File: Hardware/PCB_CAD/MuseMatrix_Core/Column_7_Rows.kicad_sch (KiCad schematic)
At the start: 46 parts, among them J14 Conn_01x03_Pin, J15 Conn_01x07_Socket, J4 Conn_01x07_Socket, Q2 2N3904, Q3 2N3904, Q4 2N3904, Q5 2N3904, Q6 2N3904, Q7 2N3904, Q8 2N3904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

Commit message: more pcb edit
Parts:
- removed J4: Conn_01x07_Socket, Connector_JST:JST_EH_B7B-EH-A_1x07_P2.50mm_Vertical, symbol Connector:Conn_01x07_Socket
- added H1, H2, H3, H4, H5, H6, H7, H8: MountingHole, MountingHole:MountingHole_2.1mm, symbol Mechanical:MountingHole
- added J13: Conn_01x10_Socket, Library:Skedd connector x10, symbol Connector:Conn_01x10_Socket
- added J17, J18: Conn_01x06_Pin, Library:Skedd connector x6, symbol Connector:Conn_01x06_Pin
- J3: renamed from J15; value Conn_01x07_Socket -> Conn_01x10_Socket; footprint Connector_JST:JST_EH_B7B-EH-A_1x07_P2.50mm_Vertical -> Library:Skedd connector x10; symbol Connector:Conn_01x07_Socket -> Connector:Conn_01x10_Socket
- R11, R12, R20, R21, R22, R6: footprint OptoDevice:R_LDR_5.1x4.3mm_P3.4mm_Vertical -> Library:LDR 2.5 horizontal
- R2: renamed from R43; footprint OptoDevice:R_LDR_5.1x4.3mm_P3.4mm_Vertical -> Library:LDR 2.5 horizontal
- R28: footprint Potentiometer_THT:Potentiometer_Bourns_PTV09A-1_Single_Vertical -> Resistor_SMD:R_0402_1005Metric
- renumbered D8 to D1, J14 to J2, Q9 to Q1, R29 to R1
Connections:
- net +3.3V: now also J17.2 (Pin_2), J18.2 (Pin_2)
- net GND: now also J17.1 (Pin_1), J18.1 (Pin_1)
- net column_voltage: now also J17.3 (Pin_3); no longer R17.1, R18.1, R19.1
- net d1: now also J13.1 (Pin_1)
- net d2: now also J13.2 (Pin_2)
- net d3: now also J13.3 (Pin_3)
- net d4: now also J13.4 (Pin_4)
- net d5 renamed d5_0
- net d5_0: now also J18.4 (Pin_4); no longer J3.5 (Pin_5)
- net d6 renamed d6_0
- net d6_0: now also J18.5 (Pin_5); no longer J3.6 (Pin_6)
- net d7 renamed d7_0
- net d7_0: now also J18.6 (Pin_6); no longer J3.7 (Pin_7)
- new net column_voltage2: J18.3 (Pin_3), R17.1, R18.1, R19.1
- new net d5_1: J13.5 (Pin_5), J17.4 (Pin_4), J3.5 (Pin_5)
- new net d6_1: J13.6 (Pin_6), J17.5 (Pin_5), J3.6 (Pin_6)
- new net d7_1: J13.7 (Pin_7), J17.6 (Pin_6), J3.7 (Pin_7)
- no-connect marks 0 -> 3

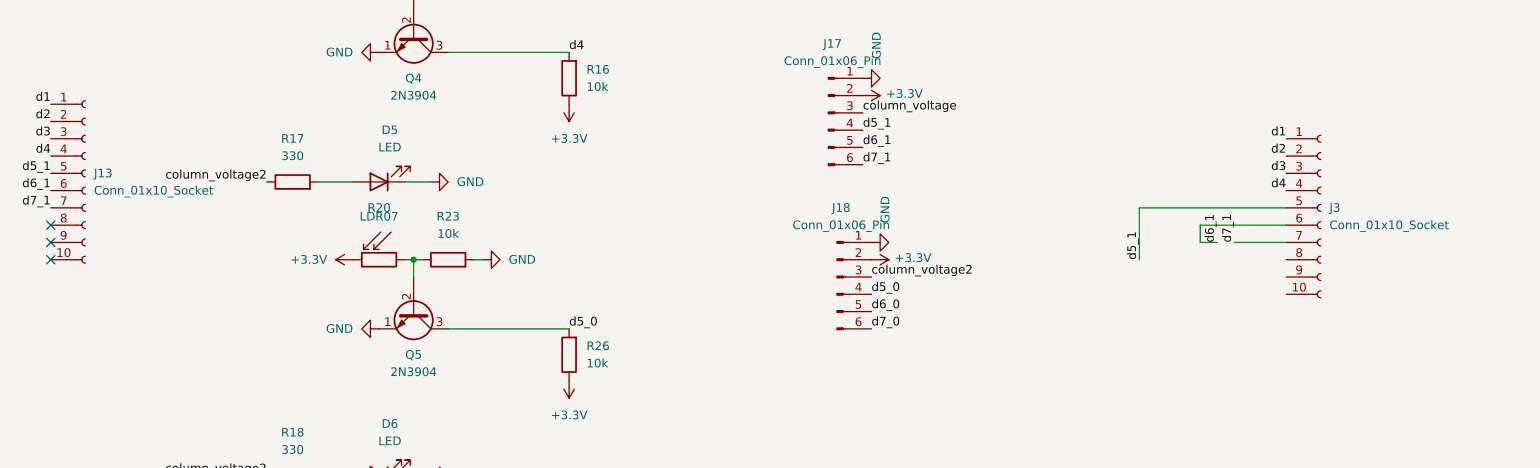
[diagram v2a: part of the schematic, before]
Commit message: separated in 2 boards
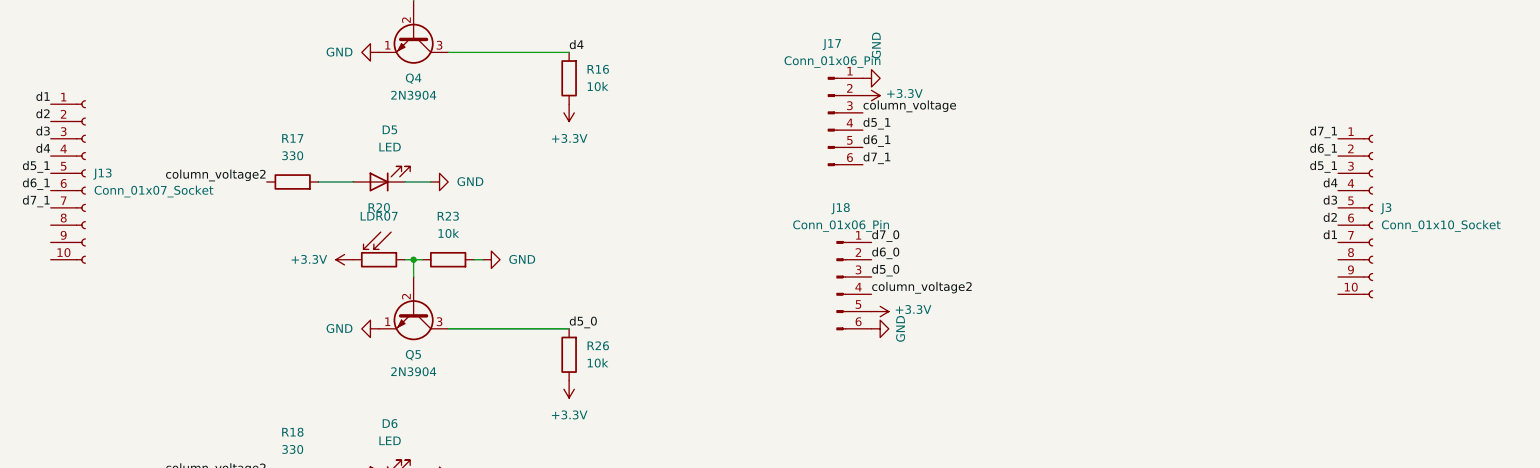
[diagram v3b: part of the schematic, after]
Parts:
- J13: value Conn_01x10_Socket -> Conn_01x07_Socket; footprint Library:Skedd connector x10 -> Connector_PinHeader_2.54mm:PinHeader_1x07_P2.54mm_Horizontal
- J17, J18: footprint Library:Skedd connector x6 -> Connector_PinHeader_2.54mm:PinHeader_1x06_P2.54mm_Horizontal
- J3: footprint Library:Skedd connector x10 -> Connector_PinHeader_2.54mm:PinHeader_1x07_P2.54mm_Horizontal
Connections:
- net +3.3V: now also J18.5 (Pin_5); no longer J18.2 (Pin_2)
- net GND: now also J18.6 (Pin_6); no longer J18.1 (Pin_1)
- net column_voltage2: now also J18.4 (Pin_4); no longer J18.3 (Pin_3)
- net d1: now also J3.7 (Pin_7); no longer J3.1 (Pin_1)
- net d2: now also J3.6 (Pin_6); no longer J3.2 (Pin_2)
- net d3: now also J3.5 (Pin_5); no longer J3.3 (Pin_3)
- net d5_0: now also J18.3 (Pin_3); no longer J18.4 (Pin_4)
- net d5_1: now also J3.3 (Pin_3); no longer J3.5 (Pin_5)
- net d6_0: now also J18.2 (Pin_2); no longer J18.5 (Pin_5)
- net d6_1: now also J3.2 (Pin_2); no longer J3.6 (Pin_6)
- net d7_0: now also J18.1 (Pin_1); no longer J18.6 (Pin_6)
- net d7_1: now also J3.1 (Pin_1); no longer J3.7 (Pin_7)
- no-connect marks 3 -> 0
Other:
- moved on the sheet: J3
